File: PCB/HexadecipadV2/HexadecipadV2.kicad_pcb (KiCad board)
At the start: 2 copper layers, 100 x 130 mm, 88 parts, among them SW1 Encoder, SW10 SW_Push_45deg, SW11 SW_Push_45deg, SW12 SW_Push_45deg, SW13 SW_Push_45deg, SW14 SW_Push_45deg, SW15 SW_Push_45deg, SW16 SW_Push_45deg, SW17 SW_Push_45deg, SW18 SW_Push_45deg, SW19 SW_Push_45deg, SW2 Encoder, SW20 SW_Push_45deg, SW21 SW_Push_45deg, SW22 SW_Push_45deg, SW23 SW_Push_45deg, SW24 SW_Push_45deg, SW25 SW_Push_45deg, SW26 SW_Push_45deg, SW27 SW_Push_45deg, SW28 SW_Push_45deg, SW3 Encoder, SW4 Encoder, SW5 SW_Push_45deg, SW6 SW_Push_45deg, SW7 SW_Push_45deg, SW8 SW_Push_45deg, SW9 SW_Push_45deg, U1 XIAO-RP2040-DIP, U2 MCP23017_SP, U3 MCP23017_SP

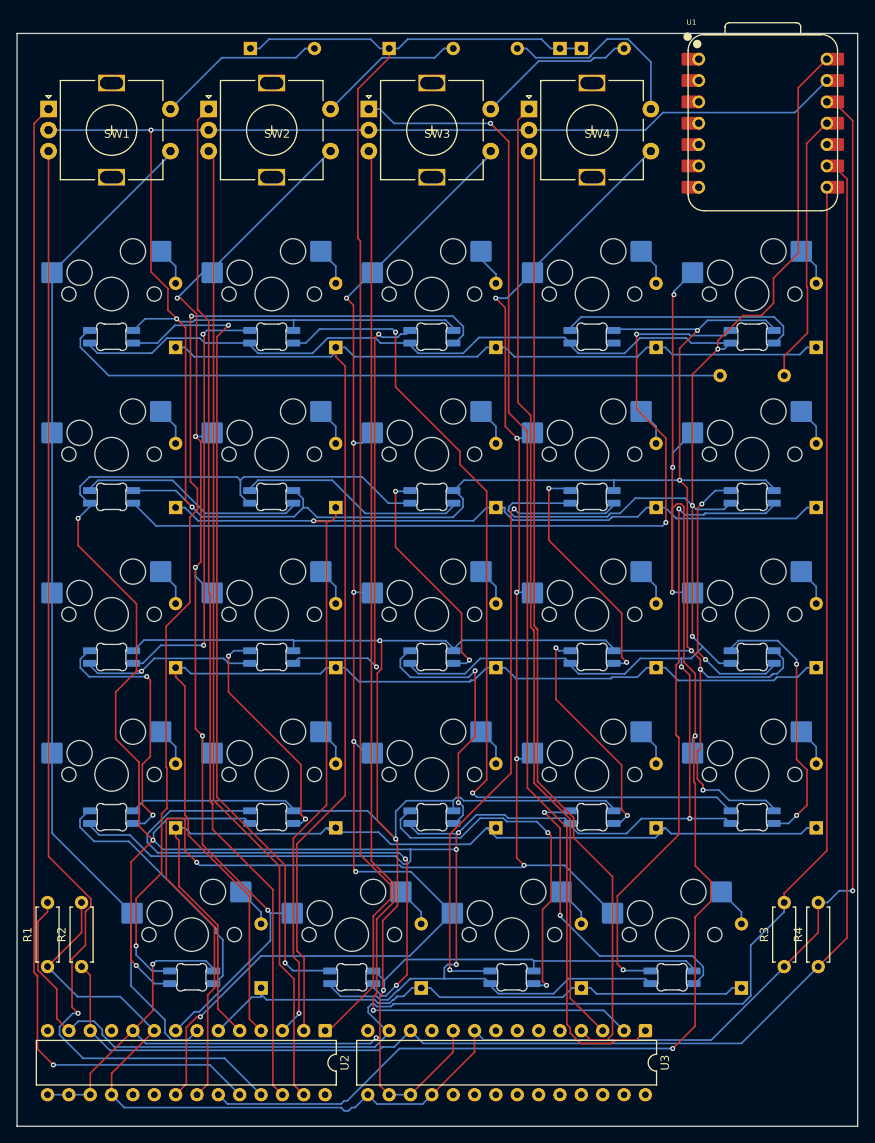
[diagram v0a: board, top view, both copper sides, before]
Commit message: Fix all traces
I stopped using freerouting because i realised it was not allowed and it was a huge pain. redid all the traces by hand and made some power planes. removed all of my LEDs because 1.21 GIGAWATTS
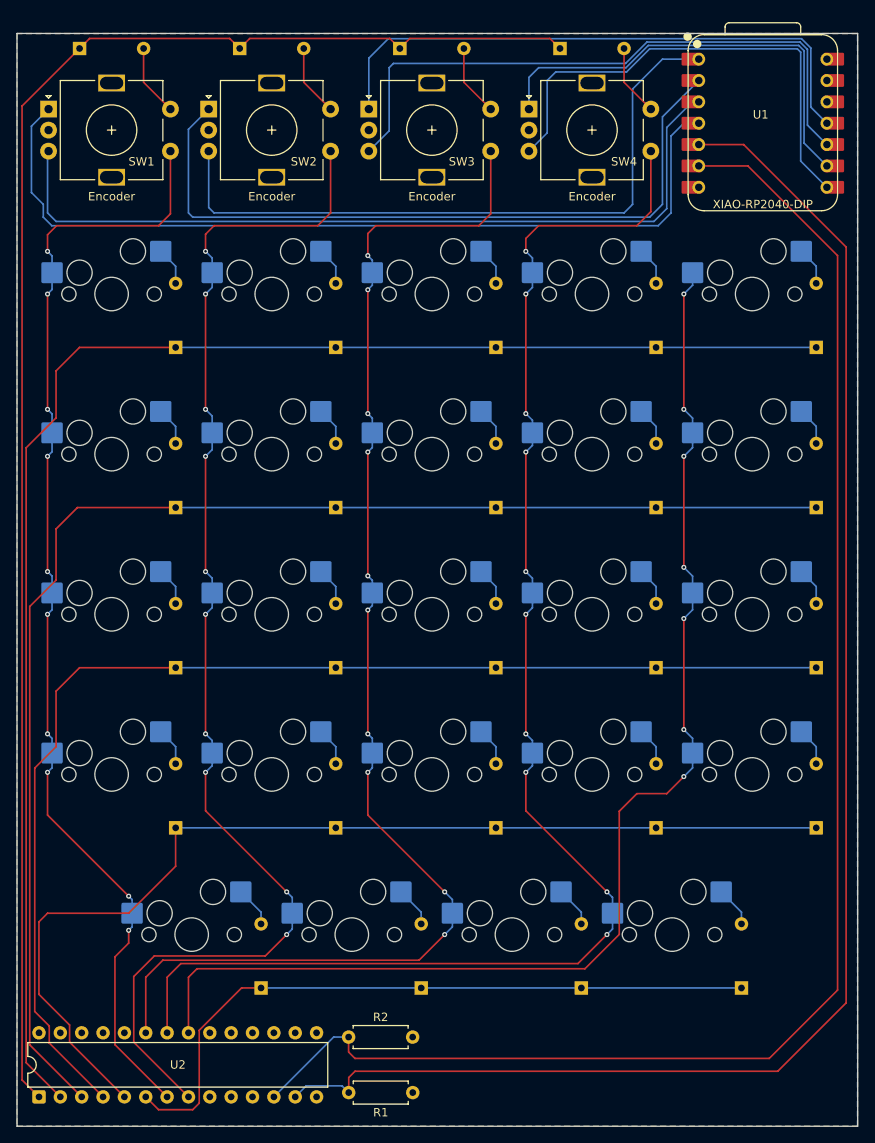
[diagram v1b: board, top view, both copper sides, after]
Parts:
- removed D29, D30, D31, D32, D33, D34, D35, D36, D37, D38, D39, D40, D41, D42, D43, D44, D45, D46, D47, D48, D49, D50, D51, D52: SK6812MINI, kicad-keyboard-parts.pretty-master:MX_SK6812MINI-E_REV
- removed R3, R4, R5: R, Resistor_THT:R_Axial_DIN0207_L6.3mm_D2.5mm_P7.62mm_Horizontal
- removed U3: MCP23017_SP, Package_DIP:DIP-28_W7.62mm
- moved R1 46.0 mm to (200.8, 149.5), turned to 180 degrees
- moved U2 34.9 mm to (156.4, 150.0), turned to 90 degrees
- moved R2 32.9 mm to (193.2, 142.9), turned to 0 degrees
- moved D28 20.3 mm to (161.2, 25.3)
- moved D26 19.1 mm to (199.3, 25.3)
- moved D27 17.8 mm to (180.2, 25.3)
- moved D25 2.54 mm to (218.3, 25.3), turned to 0 degrees
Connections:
- U1 pad 1: unconnected-(U1-GPIO26/ADC0/A0-Pad1) -> ENC2-B
- U1 pad 10: unconnected-(U1-GPIO4/MISO-Pad10) -> ENC3-B
- U1 pad 11: LEDs -> ENC3-A
- U1 pad 14: 5V -> unconnected-(U1-VBUS-Pad14)
- U1 pad 2: unconnected-(U1-GPIO27/ADC1/A1-Pad2) -> ENC2-A
- U1 pad 3: unconnected-(U1-GPIO28/ADC2/A2-Pad3) -> ENC1-B
- U1 pad 4: unconnected-(U1-GPIO29/ADC3/A3-Pad4) -> ENC1-A
- U1 pad 5: unconnected-(U1-GPIO6/SDA-Pad5) -> SDA MCP
- U1 pad 6: unconnected-(U1-GPIO7/SCL-Pad6) -> SCK MCP
- U1 pad 8: SDA MCP -> ENC4-B
- U1 pad 9: SCK MCP -> ENC4-A
- U2 pad 21: Column 2 -> Column 4
- U2 pad 23: Column 4 -> Column 2
- U2 pad 24: ENC1-A -> unconnected-(U2-GPA3-Pad24)
- U2 pad 25: ENC1-B -> unconnected-(U2-GPA4-Pad25)
- U2 pad 26: ENC2-A -> unconnected-(U2-GPA5-Pad26)
- U2 pad 27: ENC2-B -> unconnected-(U2-GPA6-Pad27)
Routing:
- net GND: track 680.7 -> 0.00 mm, vias 13 -> 0
- net 5V: track 592.2 -> 0.00 mm, vias 12 -> 0
- net 3V3: track 235.8 -> 0.02 mm, vias 1 -> 0
- net Net-(D30-DOUT): track 119.6 -> 0.00 mm, vias 2 -> 0
- net Net-(D31-DOUT): track 104.6 -> 0.00 mm, vias 2 -> 0
- net Net-(D50-DOUT): track 99.9 -> 0.00 mm, vias 2 -> 0
- net Net-(D29-DOUT): track 97.7 -> 0.00 mm, vias 2 -> 0
- net Net-(D29-DIN): track 80.1 -> 0.00 mm
- net DATA3: track 75.6 -> 0.00 mm, vias 2 -> 0
- net DATA2: track 74.5 -> 0.00 mm, vias 2 -> 0
- net ENC3-A: track 137.6 -> 69.8 mm, vias 1 -> 0
- net Net-(D34-DOUT): track 65.6 -> 0.00 mm, vias 2 -> 0
- net ENC4-A: track 114.6 -> 53.2 mm
- net ENC3-B: track 135.3 -> 74.6 mm, vias 1 -> 0
- net ENC4-B: track 113.9 -> 58.5 mm
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- added copper zone on F.Cu, net 3V3
- added copper zone on B.Cu, net GND

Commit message: make the case
took me 5 million years just to make this thing and it doesnt even look good
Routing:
- net Column 1: track 151.0 -> 148.8 mm
- net Column 3: track 174.4 -> 172.5 mm
- net Column 4: track 147.0 -> 145.2 mm
- net Column 2: track 157.0 -> 155.3 mm
- net Row 0: track 188.5 -> 187.1 mm
- net Column 0: track 135.0 -> 133.6 mm
- net SDA MCP: track 184.4 -> 183.0 mm
- net Row 3: track 144.3 -> 143.0 mm
- net SCK MCP: track 183.8 -> 182.5 mm
- net Row 4: track 124.8 -> 123.6 mm
- net ENC4-B: track 58.5 -> 57.4 mm
- net Row 1: track 181.1 -> 180.0 mm
- net ENC3-B: track 74.6 -> 73.6 mm
- net ENC1-A: track 103.1 -> 102.1 mm
- net ENC4-A: track 53.2 -> 52.2 mm
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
